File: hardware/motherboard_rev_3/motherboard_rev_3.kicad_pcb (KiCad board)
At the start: 2 copper layers, 74 parts, among them J1 Conn_ST_STDC14, J2 USB_C_Receptacle_USB2.0, J3 Conn_01x07, J4 Conn_01x03, J5 Conn_01x04, J6 Conn_01x04, U1 GPS module, U10 TPS563201, U11 INA219AIDCN, U12 TPS7A8101, U13 TCAN3403, U2 ICM-42688, U3 STM32F412CGU6, U4 BMP390, U5 BME280, U6 nRF24L01, U7 nRF24L01, U8 USBLC6-2SC6, U9 BNO055, Y1 20M

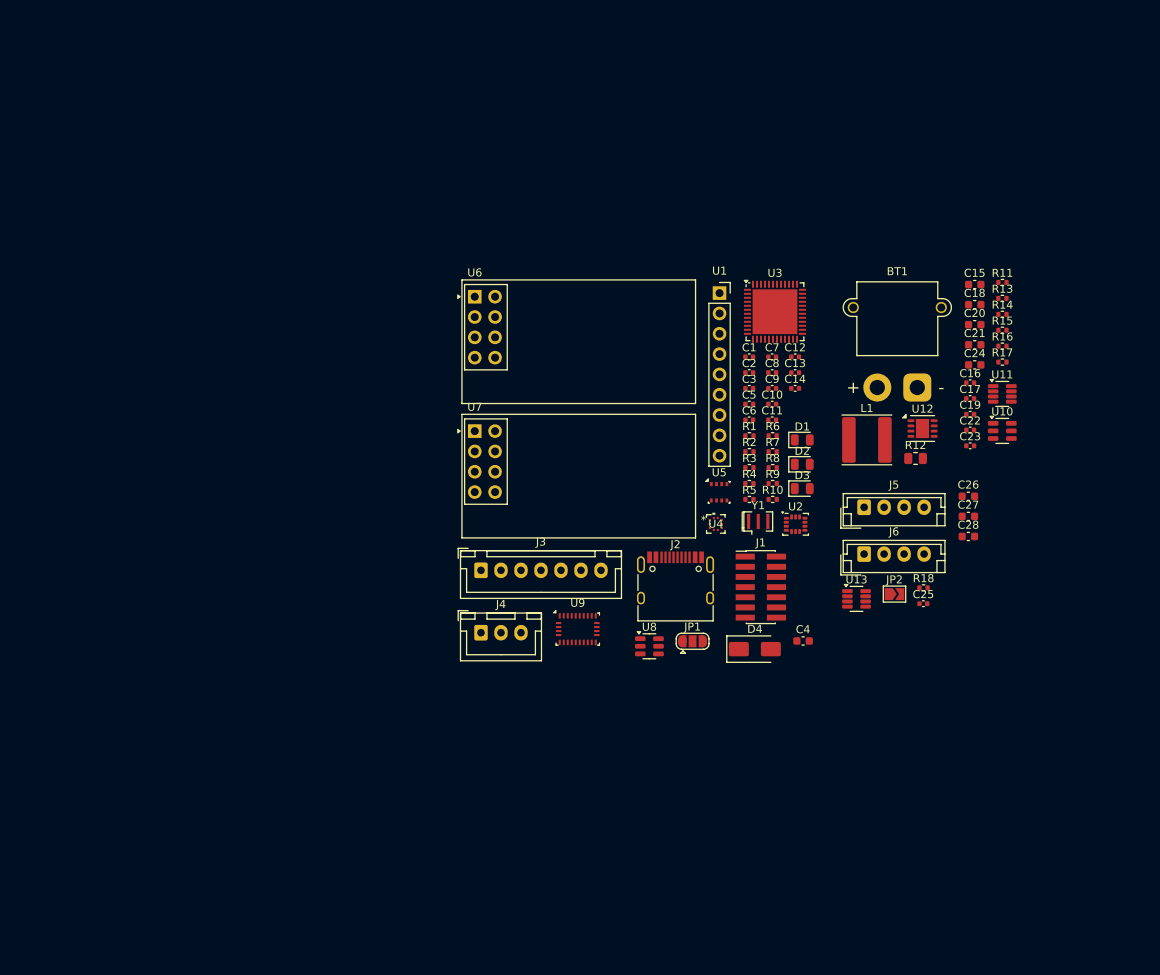
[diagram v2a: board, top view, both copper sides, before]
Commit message: Completed layout except for radio modules
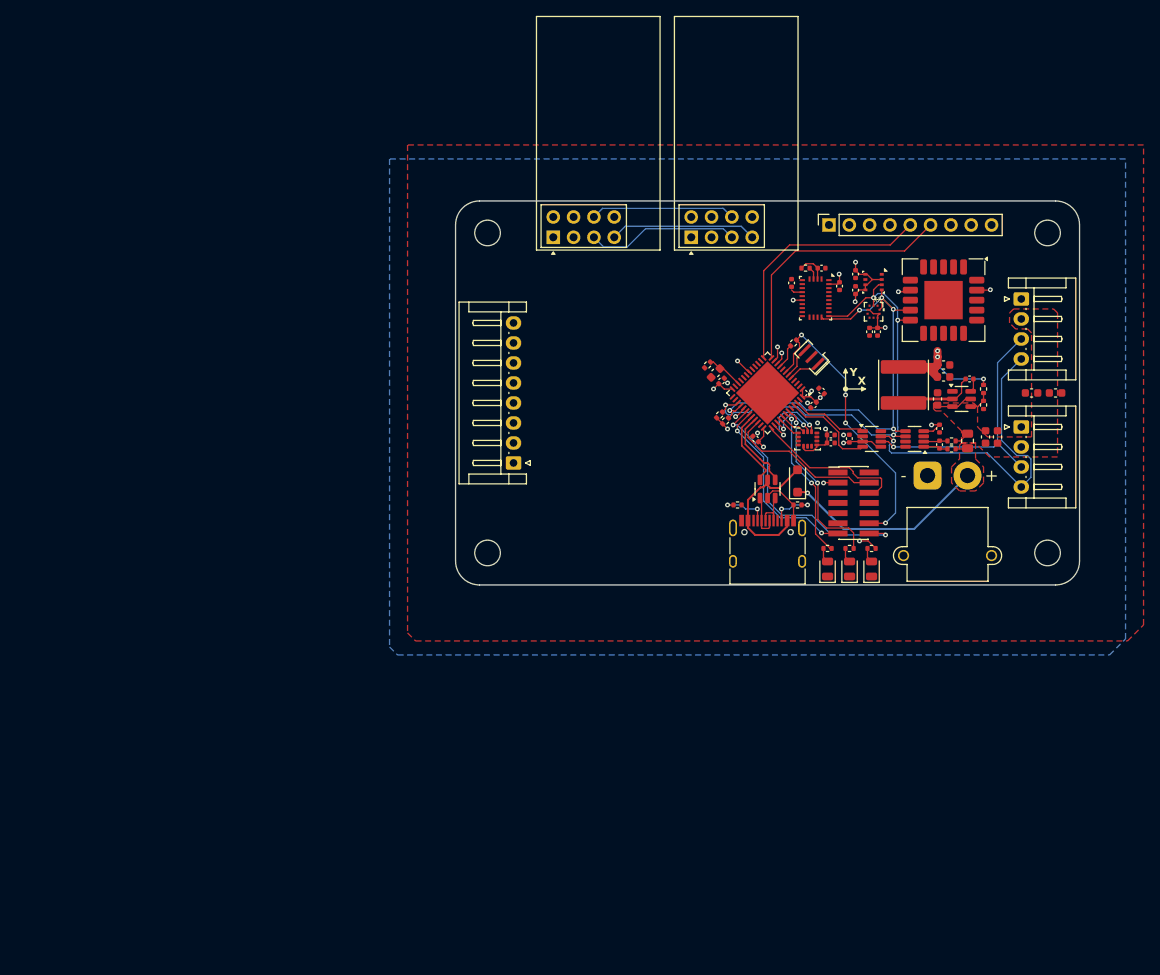
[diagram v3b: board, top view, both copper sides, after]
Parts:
- removed the C21 at (186.9, 79.0)
- removed the C22 at (186.3, 89.6)
- removed the C24 at (186.9, 81.5)
- removed C26: 10u, Capacitor_SMD:C_0603_1608Metric
- removed D4: SS34, Diode_SMD:D_SMA
- removed the J4 at (125.2, 115.0)
- removed JP1: SolderJumper_3_Open, Jumper:SolderJumper-3_P1.3mm_Open_RoundedPad1.0x1.5mm
- removed JP2: TERM, Jumper:SolderJumper-2_P1.3mm_Open_TrianglePad1.0x1.5mm
- removed R16: 30k9, Resistor_SMD:R_0402_1005Metric
- removed R17: 10k, Resistor_SMD:R_0402_1005Metric
- removed R18: 120, Resistor_SMD:R_0402_1005Metric
- removed the U12 at (180.4, 89.4)
- added C25: 10u, Capacitor_SMD:C_0603_1608Metric, F.Cu at (188.2, 90.5)
- added D5: SS14, Diode_SMD:D_SOD-123F, F.Cu at (164.8, 96.0)
- added REF**: MountingHole_3.2mm_M3, MountingHole:MountingHole_3.2mm_M3, F.Cu at (126.0, 105.0)
- added REF**: MountingHole_3.2mm_M3, MountingHole:MountingHole_3.2mm_M3, F.Cu at (196.0, 65.0)
- added REF**: MountingHole_3.2mm_M3, MountingHole:MountingHole_3.2mm_M3, F.Cu at (126.0, 65.0)
- added REF**: MountingHole_3.2mm_M3, MountingHole:MountingHole_3.2mm_M3, F.Cu at (196.0, 105.0)
- added U10: SCD41-D-R2, Sensor:Sensirion_SCD4x-1EP_10.1x10.1mm_P1.25mm_EP4.8x4.8mm, F.Cu at (183.0, 73.4)
- C23: value 470n -> 10u; footprint Capacitor_SMD:C_0402_1005Metric -> Capacitor_SMD:C_0603_1608Metric
- J3: value Conn_01x07 -> EH_S8B-EH; footprint Connector_JST:JST_XH_B7B-XH-A_1x07_P2.50mm_Vertical -> Connector_JST:JST_EH_S8B-EH_1x08_P2.50mm_Horizontal
- J5: renamed from J6; value Conn_01x04 -> EH_S4B-EH; footprint Connector_JST:JST_EH_B4B-EH-A_1x04_P2.50mm_Vertical -> Connector_JST:JST_EH_S4B-EH_1x04_P2.50mm_Horizontal
- J6: renamed from J5; value Conn_01x04 -> EH_S4B-EH; footprint Connector_JST:JST_EH_B4B-EH-A_1x04_P2.50mm_Vertical -> Connector_JST:JST_EH_S4B-EH_1x04_P2.50mm_Horizontal
- R14: renamed from R13; value 54k9 -> 33k2
- moved U9 50.9 mm to (167.0, 73.1), turned to -90 degrees
- moved C4 35.2 mm to (154.5, 82.5), turned to -135 degrees
- moved U4 33.0 mm to (174.2, 74.8), turned to -90 degrees
- moved J6 32.6 mm to (192.7, 73.2), turned to -90 degrees
- moved U5 32.6 mm to (174.2, 71.1), turned to -90 degrees
- moved U6 28.1 mm to (151.5, 65.5), turned to 90 degrees
- moved U7 26.1 mm to (134.2, 65.5), turned to 90 degrees
- moved R8 25.3 mm to (165.8, 69.4)
- moved J5 25.3 mm to (192.7, 89.2), turned to -90 degrees
- moved U8 24.6 mm to (161.0, 97.0), turned to 90 degrees
- moved C21 22.6 mm to (171.2, 90.7), turned to 90 degrees
- moved C6 22.6 mm to (172.0, 70.1), turned to -90 degrees
- moved R11 21.8 mm to (184.0, 92.0), turned to 180 degrees
- moved Y1 21.6 mm to (166.5, 80.5), turned to 135 degrees
- moved C24 21.0 mm to (197.0, 85.0)
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- renumbered C19 to C15, C17 to C16, C15 to C17, C16 to C18, C18 to C19, C25 to C21, C27 to C22, C28 to C24, BT1 to J4, R15 to R13, R14 to R15, U10 to U12
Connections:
- C17 pad 1: +BATT -> +12V
- C19 pad 1: +5V -> +3V3
- C20 pad 1: +5V -> +3V3
- C22 pad 1: +BATT -> +12V
- C23 pad 1: +3V3 -> +12V
- C23 pad 2: Net-(U12-FB) -> GND
- C24 pad 1: +BATT -> +12V
- D1 pad 1: Net-(D1-K) -> GND
- D1 pad 2: /LED_ERROR -> Net-(D1-A)
- D2 pad 1: Net-(D2-K) -> GND
- D2 pad 2: /LED_IND -> Net-(D2-A)
- D3 pad 1: Net-(D3-K) -> GND
- D3 pad 2: /LED_HRTBT -> Net-(D3-A)
- J2 pad A6: /PORT- -> /PORT+
- J2 pad A7: /PORT+ -> /PORT-
- J2 pad B6: /PORT- -> /PORT+
- J2 pad B7: /PORT+ -> /PORT-
- J3 pad 7: Net-(J3-Pin_7) -> /PWM_{IN}
- J4 pad 1: Net-(BT1-+) -> GND
- J4 pad 2: GND -> +BATT
- J5 pad 2: +BATT -> +12V
- J6 pad 2: +BATT -> +12V
- L1 pad 2: +5V -> +3V3
- R11 pad 1: Net-(BT1-+) -> +BATT
- R12 pad 1: Net-(BT1-+) -> +BATT
- R12 pad 2: +BATT -> +12V
- R13 pad 1: +BATT -> +12V
- R14 pad 1: +5V -> +3V3
- R5 pad 1: GND -> Net-(D1-A)
- R5 pad 2: Net-(D1-K) -> /LED_ERROR
- R6 pad 1: GND -> Net-(D2-A)
- R6 pad 2: Net-(D2-K) -> /LED_IND
- R7 pad 1: Net-(D3-K) -> Net-(D3-A)
- R7 pad 2: GND -> /LED_HRTBT
- U1 pad 1: +3V3 -> unconnected-(U1-3.3V-Pad1)
- U12 pad 3: +BATT -> +12V
- U12 pad 5: +BATT -> +12V
- U3 pad 1: unconnected-(U3-VBAT-Pad1) -> +3V3
- U3 pad 10: /CO_{2} -> /PWM_{IN}
- U8 pad 1: /PORT+ -> /PORT-
- U8 pad 3: /PORT- -> /PORT+
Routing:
- net +3V3: track 0.00 -> 83.5 mm, vias 0 -> 18
- net /SDA: track 0.00 -> 59.8 mm, vias 0 -> 4
- net /SCL: track 0.00 -> 59.3 mm, vias 0 -> 5
- net /CAN/CANH: track 0.00 -> 41.5 mm, vias 0 -> 1
- net /~{RST}: track 0.00 -> 36.7 mm, vias 0 -> 4
- net /CAN/CANL: track 0.00 -> 33.5 mm, vias 0 -> 1
- net /LED_HRTBT: track 0.00 -> 33.3 mm, vias 0 -> 2
- net /GPS_RX: track 0.00 -> 32.8 mm
- net /DEBUG_TX: track 0.00 -> 32.7 mm, vias 0 -> 2
- net /GPS_TX: track 0.00 -> 31.6 mm
- net +BATT: track 0.00 -> 27.4 mm, vias 0 -> 1
- net /DEBUG_RX: track 0.00 -> 23.9 mm, vias 0 -> 2
- net /LED_IND: track 0.00 -> 22.3 mm, vias 0 -> 2
- net /SWDIO: track 0.00 -> 19.9 mm
- net /SWCLK: track 0.00 -> 19.5 mm
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- added copper zone on F.Cu, net +12V
- added copper zone on B.Cu, net +3V3
- added copper zone on F.Cu, net +BATT
- added copper zone on F.Cu, net GND
- added copper zone on In1.Cu, net GND
- added copper zone on In2.Cu, net GND
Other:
- board outline added: 78 x 48 mm
- copper layers 2 -> 4
- board text added: "ICM-42688 must be 90 deg CCW to BNO055 to align axes"
- board text added: "SPACE FOR FUTURE RADIO CIRCUITS"
- board text added: "X"
- board text added: "Y"

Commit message: Motherboard rev 3.1 as ordered
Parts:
- J2: value USB_C_Receptacle_USB2.0 -> USB4105-GF-A-120; footprint Connector_USB:USB_C_Receptacle_HRO_TYPE-C-31-M-12 -> Connector_USB:USB_C_Receptacle_GCT_USB4105-xx-A_16P_TopMnt_Horizontal
- moved C14 0.25 mm to (164.0, 71.5)
- moved J2 0.25 mm to (161.0, 105.2)
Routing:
- net /RADIO_INT_CE: track 0.00 -> 39.6 mm, vias 0 -> 2
- net /PWM_{IN}: track 1.57 -> 37.1 mm, vias 1 -> 2
- net /RADIO_INT_IRQ: track 0.00 -> 34.5 mm, vias 0 -> 2
- net /RADIO_INT_CS: track 0.00 -> 33.8 mm
- net /ENC4: track 0.00 -> 31.0 mm
- net /ENC5: track 0.00 -> 30.8 mm
- net /ENC1: track 1.54 -> 30.7 mm, vias 1 -> 2
- net /ENC2: track 0.00 -> 29.0 mm
- net /ENC3: track 0.00 -> 27.7 mm
- net /RADIO_EXT_CS: track 0.00 -> 26.9 mm
- net /RADIO_EXT_IRQ: track 0.00 -> 25.2 mm, vias 0 -> 1
- net /RADIO_{SCK}: track 19.1 -> 40.5 mm
- net /RADIO_{MOSI}: track 18.1 -> 39.1 mm
- net /RADIO_EXT_CE: track 1.90 -> 19.0 mm, vias 1 -> 2
- net /RADIO_{MISO}: track 19.2 -> 35.8 mm
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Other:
- board text added: "0"
- board text added: "0 mm"
- board text added: "0.01 mm"
- board text added: "0.02"
- board text added: "0.035 mm"
- board text added: "0.1 mm"
- board text added: "0.1500 mm / 0.1500 mm"
- board text added: "0.3000 mm"
- board text added: "1"
- board text added: "1.24 mm"
- board text added: "1.6000 mm"
- board text added: "3.3"
- board text added: "4"
- board text added: "4.5"
- board text added: "78.0000 mm x 48.0000 mm"
- board text added: "<17V"
- board text added: "B.Cu"
- board text added: "B.Mask"
- board text added: "B.Paste"
- board text added: "B.Silkscreen"
- board text added: "BOARD CHARACTERISTICS"
- board text added: "Board Thickness:"
- board text added: "Board overall dimensions:"
- board text added: "Bottom Silk Screen"
- board text added: "Bottom Solder Mask"
- board text added: "Bottom Solder Paste"
- board text added: "CAN"
- board text added: "Castellated pads:"
- board text added: "Color"
- board text added: "Copper Finish:"
- board text added: "Copper Layer Count:"
- board text added: "Dielectric"
- board text added: "ENCODER"
- board text added: "EXTERNAL"
- board text added: "Edge card connectors:"
- board text added: "Epsilon R"
- board text added: "F.Cu"
- board text added: "F.Mask"
- board text added: "F.Paste"
- board text added: "F.Silkscreen"
- board text added: "FALCON MOTHERBOARD REV. ${REVISION}"
- board text added: "FR4"
- board text added: "FR4 natural"
- board text added: "GPS"
- board text added: "Green"
- board text added: "HAL SnPb"
- board text added: "INTERNAL"
- board text added: "Impedance Control:"
- board text added: "In1.Cu"
- board text added: "In2.Cu"
- board text added: "JLCJLCJLCJLC"
- board text added: "Layer Name"
- board text added: "Loss Tangent"
- board text added: "Material"
- board text added: "Min hole diameter:"
- board text added: "Min track/spacing:"
- board text added: "No"
- board text added: "Not specified"
- board text added: "Plated Board Edge:"
- board text added: "SB"
- board text added: "THIS SIDE TO MOUNTING SURFACE"
- board text added: "Thickness (mm)"
- board text added: "Top Silk Screen"
- board text added: "Top Solder Mask"
- board text added: "Top Solder Paste"
- board text added: "Type"
- board text added: "White"
- board text added: "copper"
- board text added: "core"
- board text added: "prepreg"
